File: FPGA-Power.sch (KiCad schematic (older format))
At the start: 26 parts, among them U30 10CL025YU256C8G

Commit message: PVT
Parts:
- R77: renamed from R87; value 0 -> DNP(0)
- R78: renamed from R88; value DNP(0) -> 1; PartName RK73Z1ETTP -> RK73B1ETTP1R0J
- renumbered C106 to C101, C107 to C102, C108 to C103, C109 to C104, C110 to C105, C111 to C106, C112 to C107, C113 to C108, C114 to C109, C115 to C110, C116 to C111, C117 to C112, C118 to C113, C119 to C114, C120 to C115, C121 to C116, C122 to C117, C123 to C118, C124 to C119, C125 to C120, C126 to C121, C127 to C122, L11 to L7, U30 to U28
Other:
- note added: "<-Jumper"

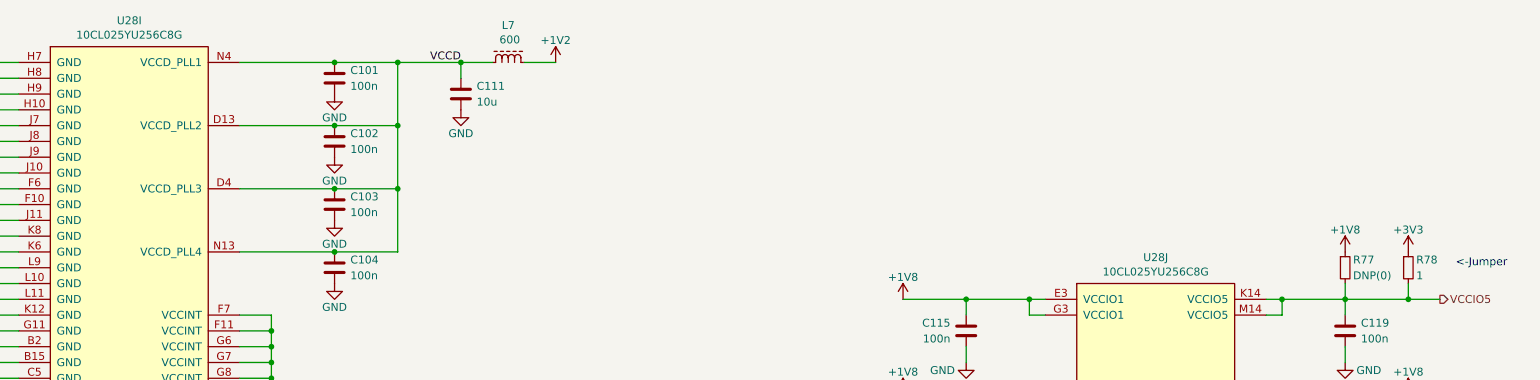
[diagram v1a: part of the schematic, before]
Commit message: SBUにTVSダイオードを追加
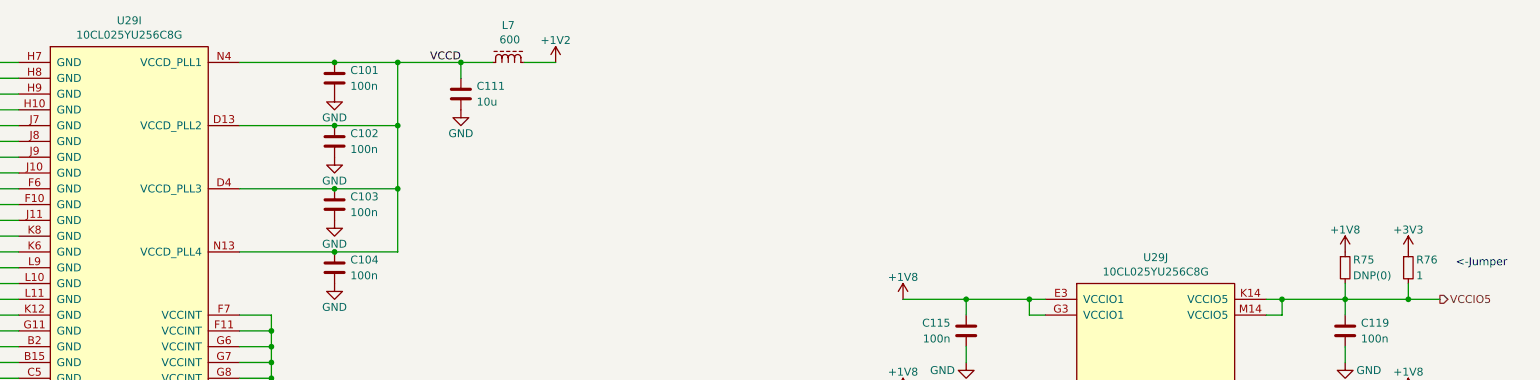
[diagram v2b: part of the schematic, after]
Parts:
- renumbered R77 to R75, R78 to R76, U28 to U29
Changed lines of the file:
@@
 P 2000 3500
 AR Path="/5E4B5786/5E50CAC5" Ref="U?"  Part="9"
-AR Path="/5E4B5786/5E4FDC2D/5E50CAC5" Ref="U28"  Part="9"
+AR Path="/5E4B5786/5E4FDC2D/5E50CAC5" Ref="U29"  Part="9"
 AR Path="/5E50CAC5" Ref="U?"  Part="9"
-F 0 "U28" H 2000 6165 50  0000 C CNN
+F 0 "U29" H 2000 6165 50  0000 C CNN
 F 1 "10CL025YU256C8G" H 2000 6074 50  0000 C CNN
 F 2 "Phoenix:BGA256_14.0x14.0_P0.8" H 2000 3500 50  0001 C CNN
@@
 P 8500 3500
 AR Path="/5E4B5786/5E50CACB" Ref="U?"  Part="10"
-AR Path="/5E4B5786/5E4FDC2D/5E50CACB" Ref="U28"  Part="10"
+AR Path="/5E4B5786/5E4FDC2D/5E50CACB" Ref="U29"  Part="10"
 AR Path="/5E50CACB" Ref="U?"  Part="10"
-F 0 "U28" H 8500 4665 50  0000 C CNN
+F 0 "U29" H 8500 4665 50  0000 C CNN
 F 1 "10CL025YU256C8G" H 8500 4574 50  0000 C CNN
 F 2 "Phoenix:BGA256_14.0x14.0_P0.8" H 8500 3500 50  0001 C CNN
@@
 $EndComp
 $Comp
-L passive:R R77
+L passive:R R75
 U 1 1 5F12C54A
 P 9700 2400
-F 0 "R77" H 9750 2450 50  0000 L CNN
+F 0 "R75" H 9750 2450 50  0000 L CNN
 F 1 "DNP(0)" H 9750 2350 50  0000 L CNN
 F 2 "Resistor-Chip:R_CHIP_1005_Hand_NoSilk" V 9750 2300 50  0001 C CNN
@@
 $EndComp
 $Comp
-L passive:R R78
+L passive:R R76
 U 1 1 5F1713F5
 P 10100 2400
-F 0 "R78" H 10150 2450 50  0000 L CNN
+F 0 "R76" H 10150 2450 50  0000 L CNN
 F 1 "1" H 10150 2350 50  0000 L CNN
 F 2 "Resistor-Chip:R_CHIP_1005_Hand_NoSilk" V 10150 2300 50  0001 C CNN
